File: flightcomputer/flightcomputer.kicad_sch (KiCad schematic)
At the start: 87 parts, among them J1 Conn_Coaxial, J10 Conn_01x03, J11 Conn_01x03, J12 M20-6102045, J13 Conn_01x07, J2 Conn_Coaxial, J3 Conn_Coaxial, J4 Conn_Coaxial, J5 S3B-PH-K-S-GW, J6 S3B-PH-K-S-GW, J7 S4B-PH-K-S_LF__SN_, J8 S3B-PH-K-S-GW, J9 Conn_01x06, U1 MAX-M10S, U2 LIS2MDLTR, U3 BMI088, U4 MS5607-02BA, U5 ESP32-S3-WROOM-1-N4, U7 Teensy4.1, U8 LSM6DSO32TR, U9 RFM96W-433S2

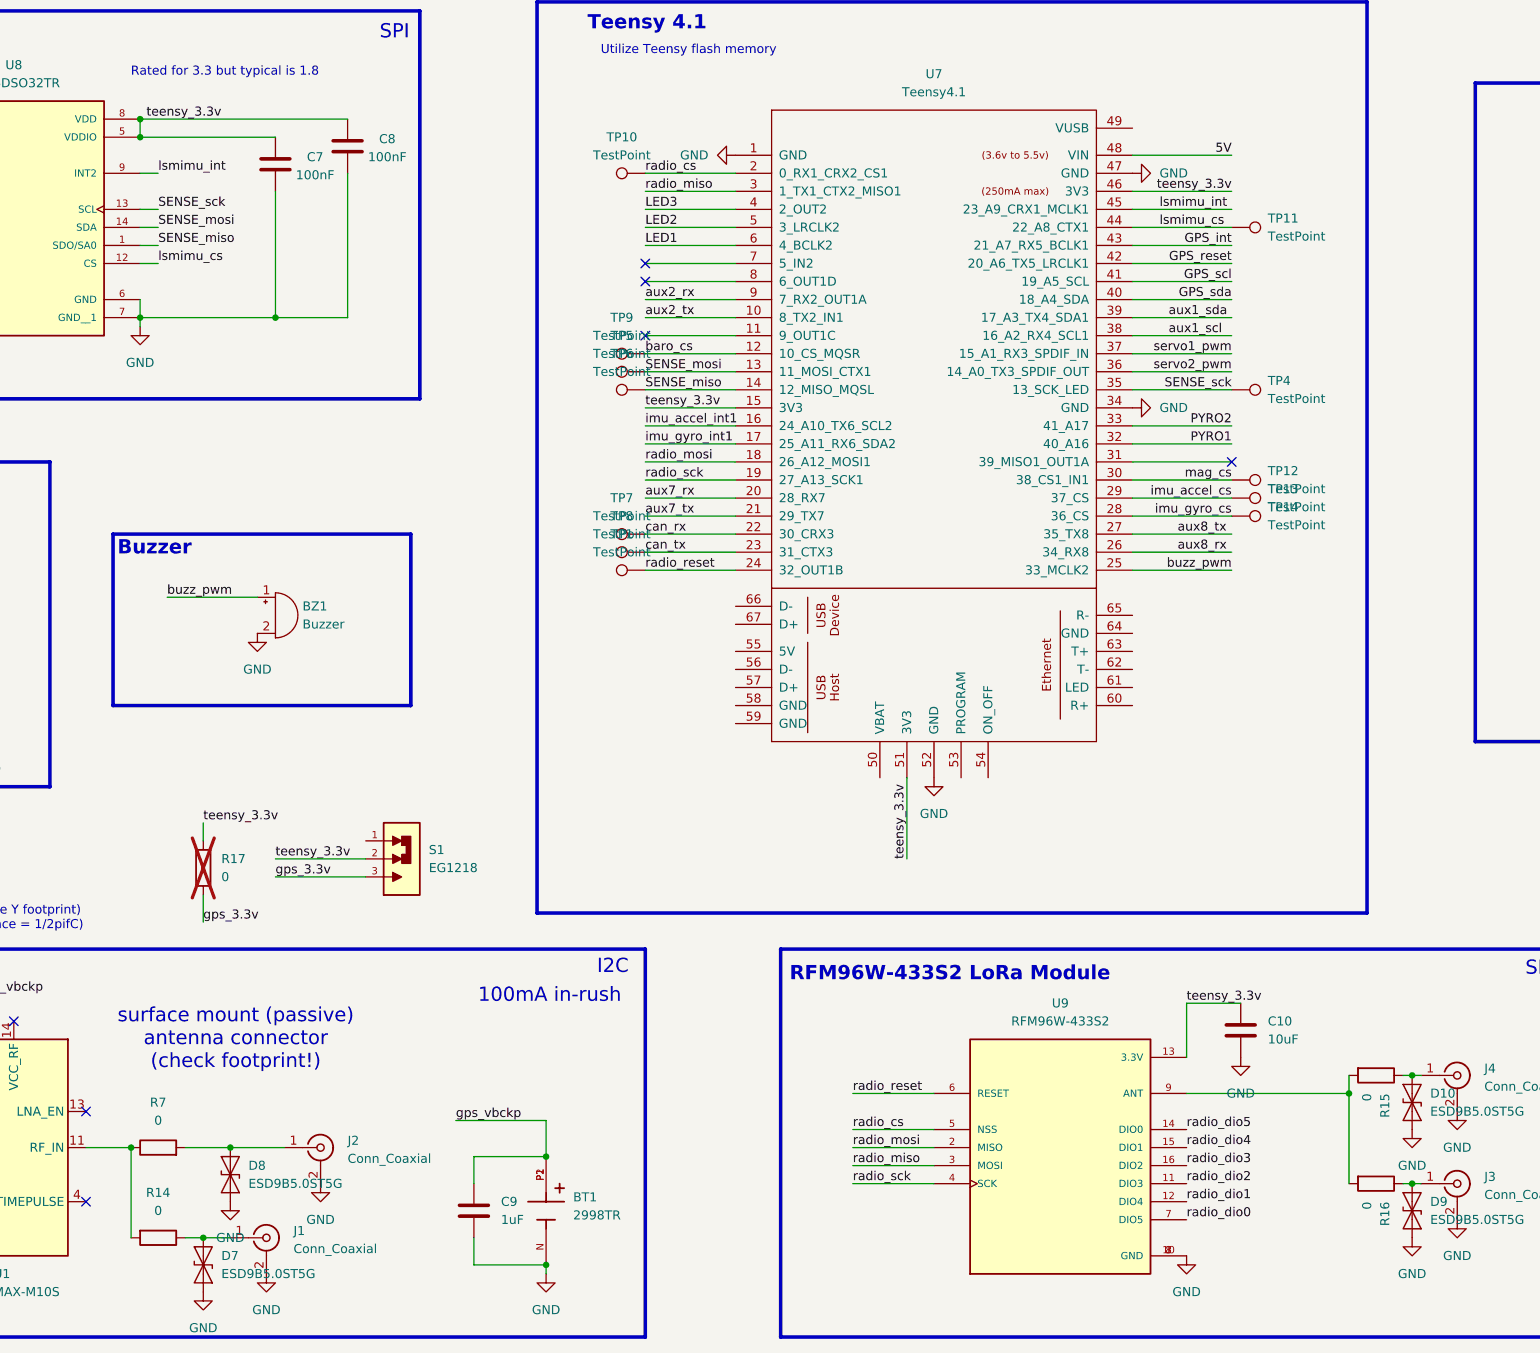
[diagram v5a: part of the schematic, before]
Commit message: Y 0ohm for antenna selection
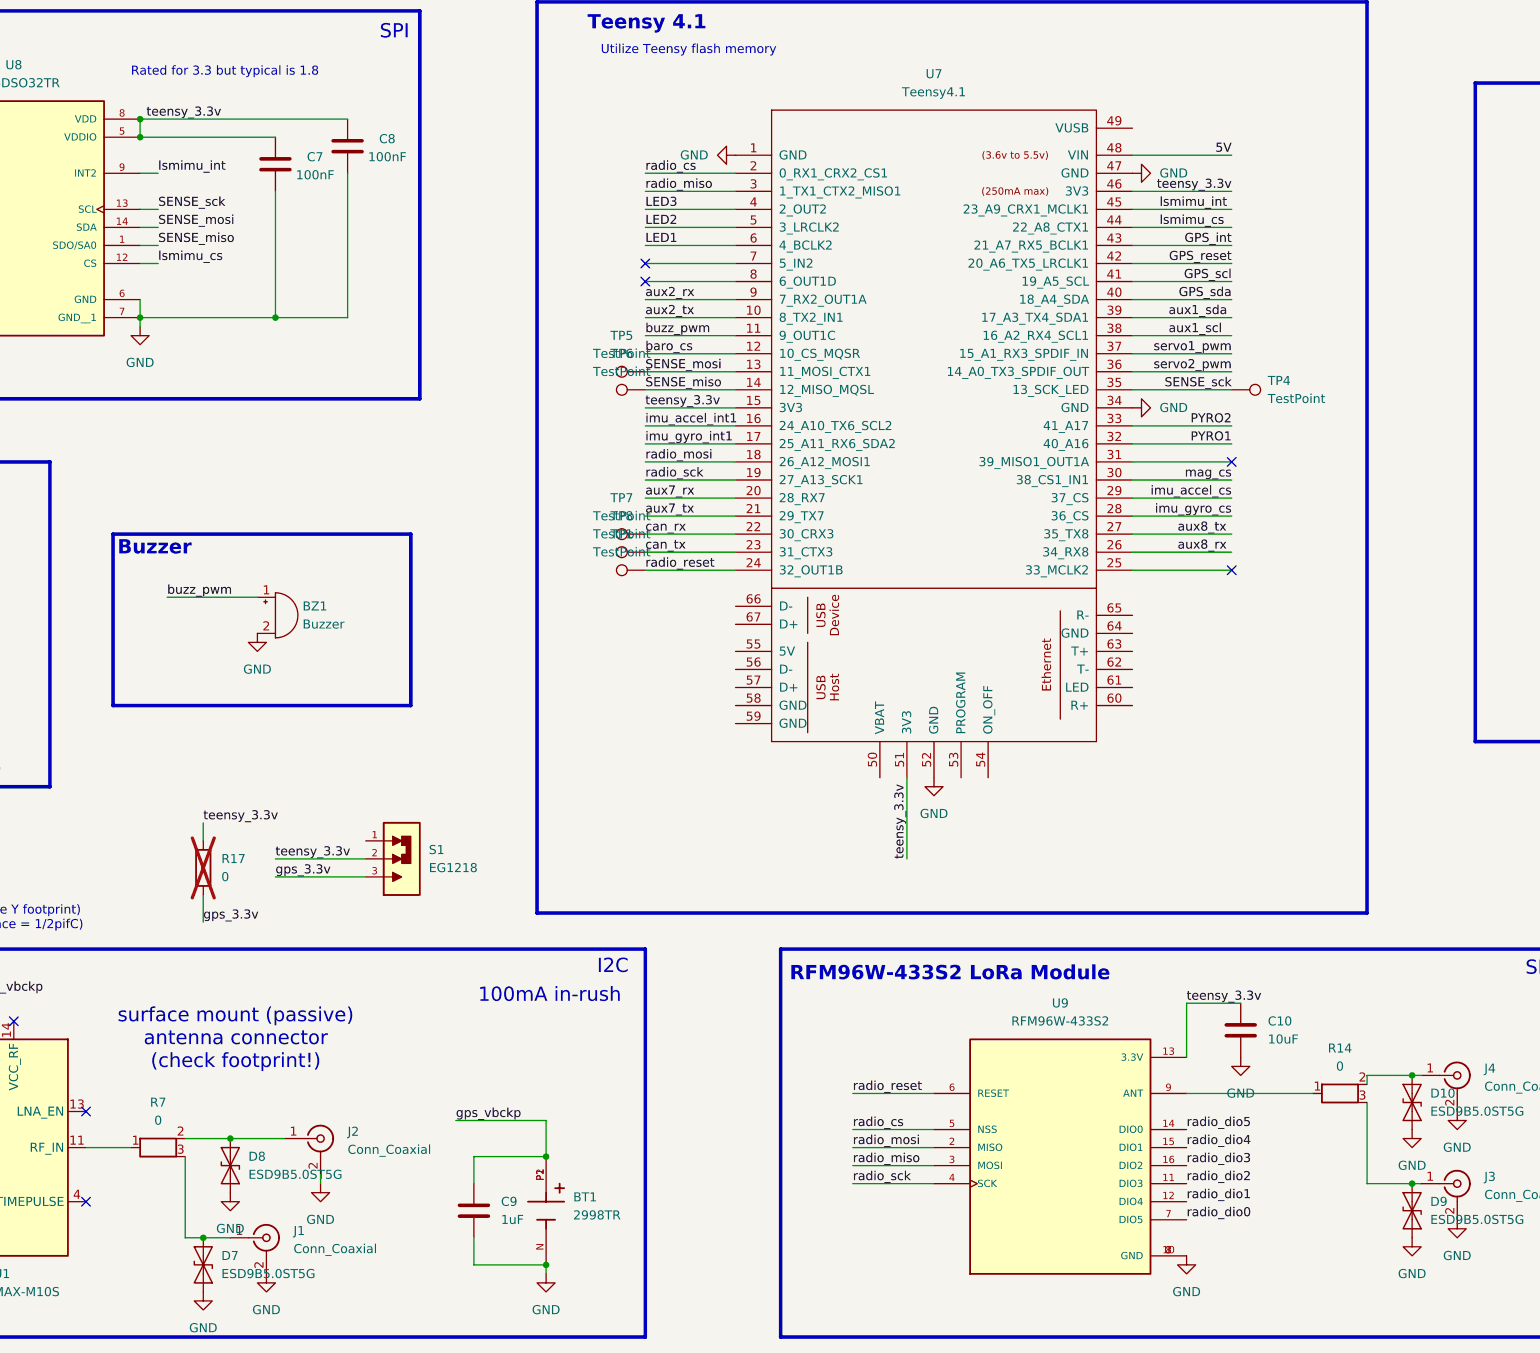
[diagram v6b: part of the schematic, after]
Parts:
- removed R14, R15, R16, R7: 0, Resistor_SMD:R_0603_1608Metric_Pad0.98x0.95mm_HandSolder, symbol Device:R
- removed TP10, TP11, TP12, TP13, TP14, TP9: TestPoint, Connector_PinHeader_2.54mm:PinHeader_1x01_P2.54mm_Vertical, symbol Connector:TestPoint
- added R14, R7: 0, HPRlibrary:RES_0OHM_Y, symbol HPRlibrary:RES_0OHM_Y
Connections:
- net buzz_pwm: now also U7.11 (9_OUT1C); no longer U7.25 (33_MCLK2)
- net at D7.2 (A2), J1.1 (In): now also R7.3
- net at U1.11 (RF_IN): now also R7.1
- net at D10.2 (A2), J4.1 (In): now also R14.2
- net at U9.9 (ANT): now also R14.1
- net at D9.2 (A2), J3.1 (In): now also R14.3
- net at D8.2 (A2), J2.1 (In): now also R7.2
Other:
- moved on the sheet: D8, J2

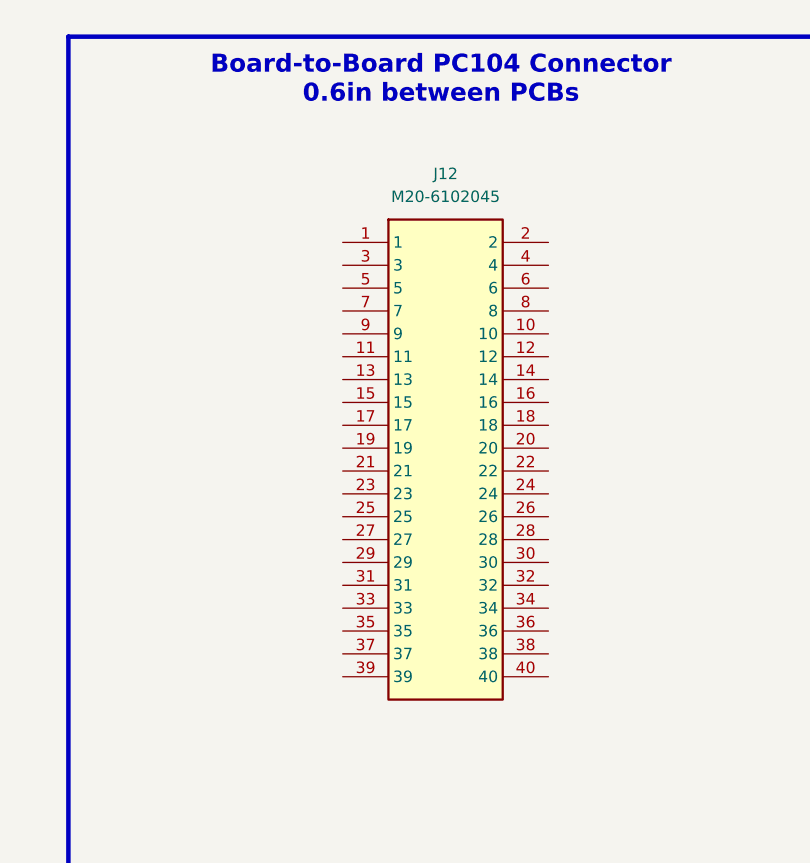
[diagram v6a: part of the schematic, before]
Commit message: fc new connector
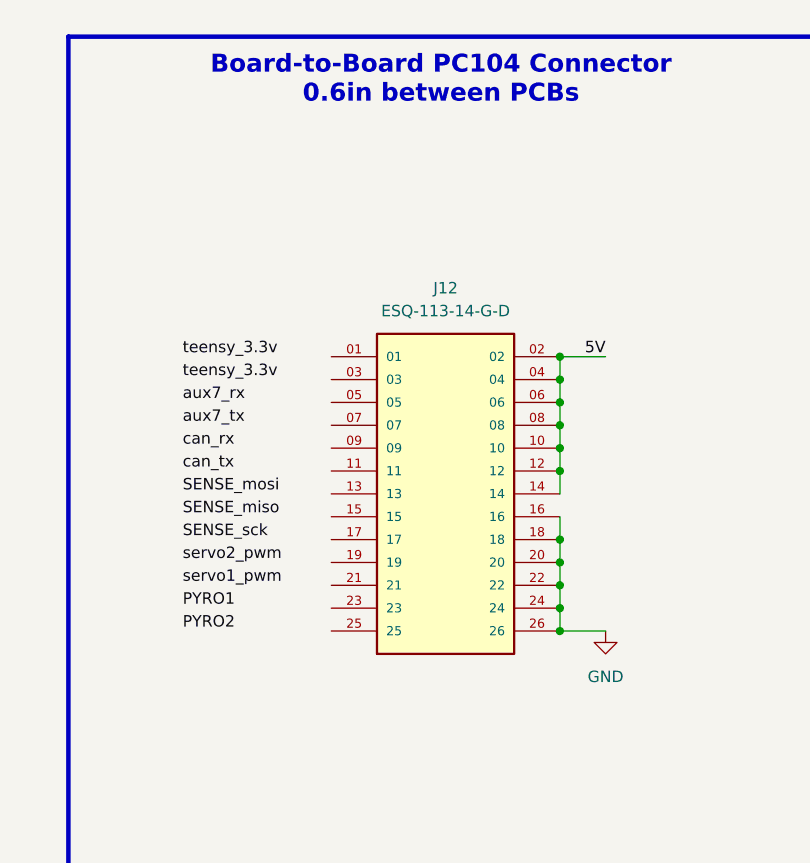
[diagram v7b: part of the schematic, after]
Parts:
- removed J12: M20-6102045, HPRlibrary:RHDR40W66P254_2X20_5146X500X1105P, symbol HPRsymbols:M20-6102045
- added J12: ESQ-113-14-G-D, HPRlibrary:SAMTEC_ESQ-113-14-G-D, symbol HPRlibrary:ESQ-113-14-G-D
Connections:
- net 5V: now also J12.02, J12.04, J12.06, J12.08, J12.10, J12.12, J12.14
- net GND: now also J12.16, J12.18, J12.20, J12.22, J12.24, J12.26

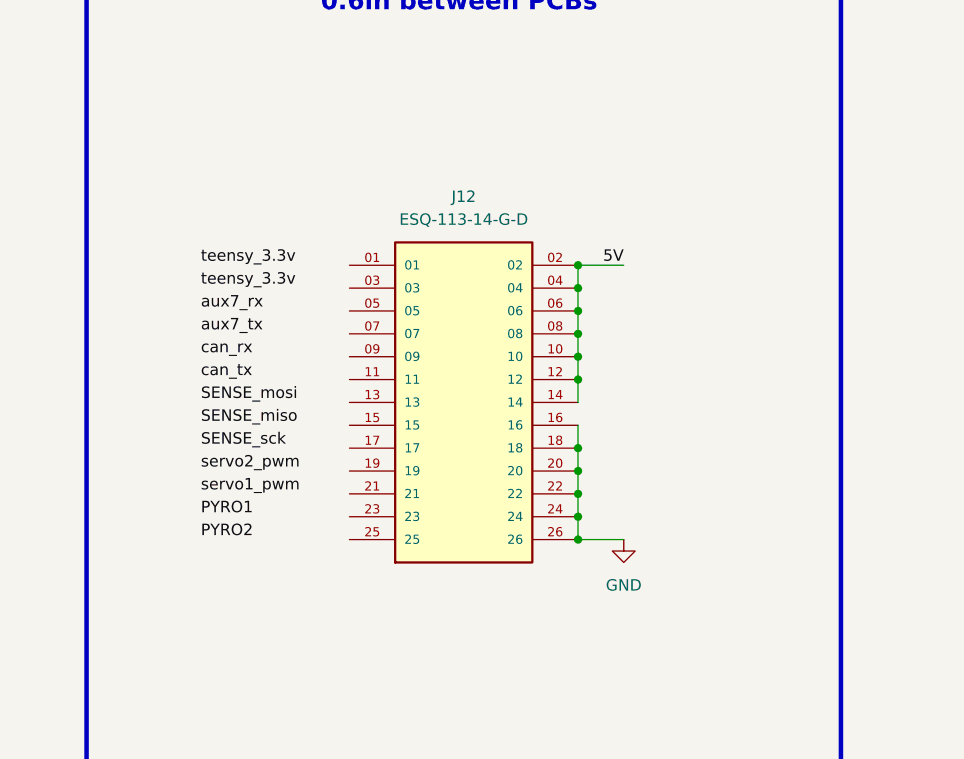
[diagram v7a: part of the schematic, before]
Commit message: connector nets
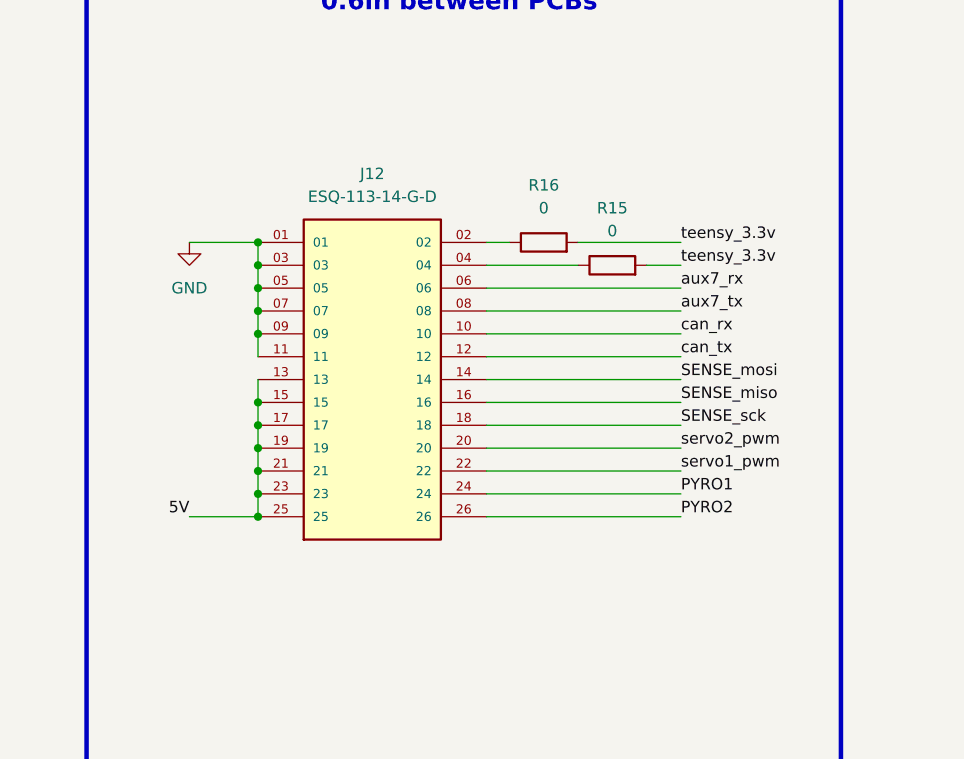
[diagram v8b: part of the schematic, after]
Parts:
- added R15, R16: 0, Resistor_SMD:R_0603_1608Metric_Pad0.98x0.95mm_HandSolder, symbol Device:R
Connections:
- net 5V: now also J12.13, J12.15, J12.17, J12.19, J12.21, J12.23, J12.25; no longer J12.02, J12.04, J12.06, J12.08, J12.10, J12.12, J12.14
- net GND: now also J12.01, J12.03, J12.05, J12.07, J12.09, J12.11; no longer J12.16, J12.18, J12.20, J12.22, J12.24, J12.26
- net PYRO1: now also J12.24
- net PYRO2: now also J12.26
- net SENSE_miso: now also J12.16
- net SENSE_mosi: now also J12.14
- net SENSE_sck: now also J12.18
- net aux7_rx: now also J12.06
- net aux7_tx: now also J12.08
- net can_rx: now also J12.10
- net can_tx: now also J12.12
- net servo1_pwm: now also J12.22
- net servo2_pwm: now also J12.20
- net teensy_3.3v: now also R15.2, R16.2
- new net: J12.02, R16.1
- new net: J12.04, R15.1
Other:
- moved on the sheet: J12
